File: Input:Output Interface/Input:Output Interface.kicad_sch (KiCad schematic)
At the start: 25 parts, among them J1 Conn_01x03_Male, J2 Conn_01x03_Male, J3 16-way-pcb-edge-Educ-8-connec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, J4 16-way-pcb-edge-Educ-8-connec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, U1 74LS37, U10 74LS01, U11 74LS04, U2 74LS04, U3 7400, U4 74LS04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

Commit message: Schematic update 2024-04-14 plus fixes
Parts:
- C1, C2, C3, C4: value C -> 47nF
- H1, H2: symbol Input:Output-Interface-rescue:Card_handle-EDUC-8 -> EDUC8:Card_handle-EDUC-8
- J3, J4: symbol Input:Output-Interface-rescue:16-way-pcb-edge-Educ-8-connectors-EDUC-8 -> EDUC8:16-way-pcb-edge-Educ-8-connectors-EDUC-8
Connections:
- net I_O_DEVICE_SELECT: now also U3.1, U3.9; no longer U3.12, U3.5
- new net: U2.4, U3.12, U3.5
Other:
- note added: "00"
- note added: "01"
- note added: "10"
- note added: "11"
- note added: "606"
- note added: "616"
- note added: "626"
- note added: "636"
- note added: "C1 47nF C2 47nF C3 47nF C4 47nF H1 Card_handle H2 Card_handle J1 Conn_01x03_Male J2 Conn_01x03_Male J3 16-way-pcb-edge J4 16-way-pcb-edge R1 1K R2 1K R3 1K R4 1K U1 74LS37 U2 74LS04 U3 74LS00 U4 74LS04 U5 74LS00 U6 74LS37 U7 74LS37 U8 74LS01 U9 74LS00 U10 74LS01 U11 74LS04"
- note added: "DATA"
- note added: "c"
- moved on the sheet: C1, C2, C3, C4, H1, H2, J3, J4, U2B, U3D

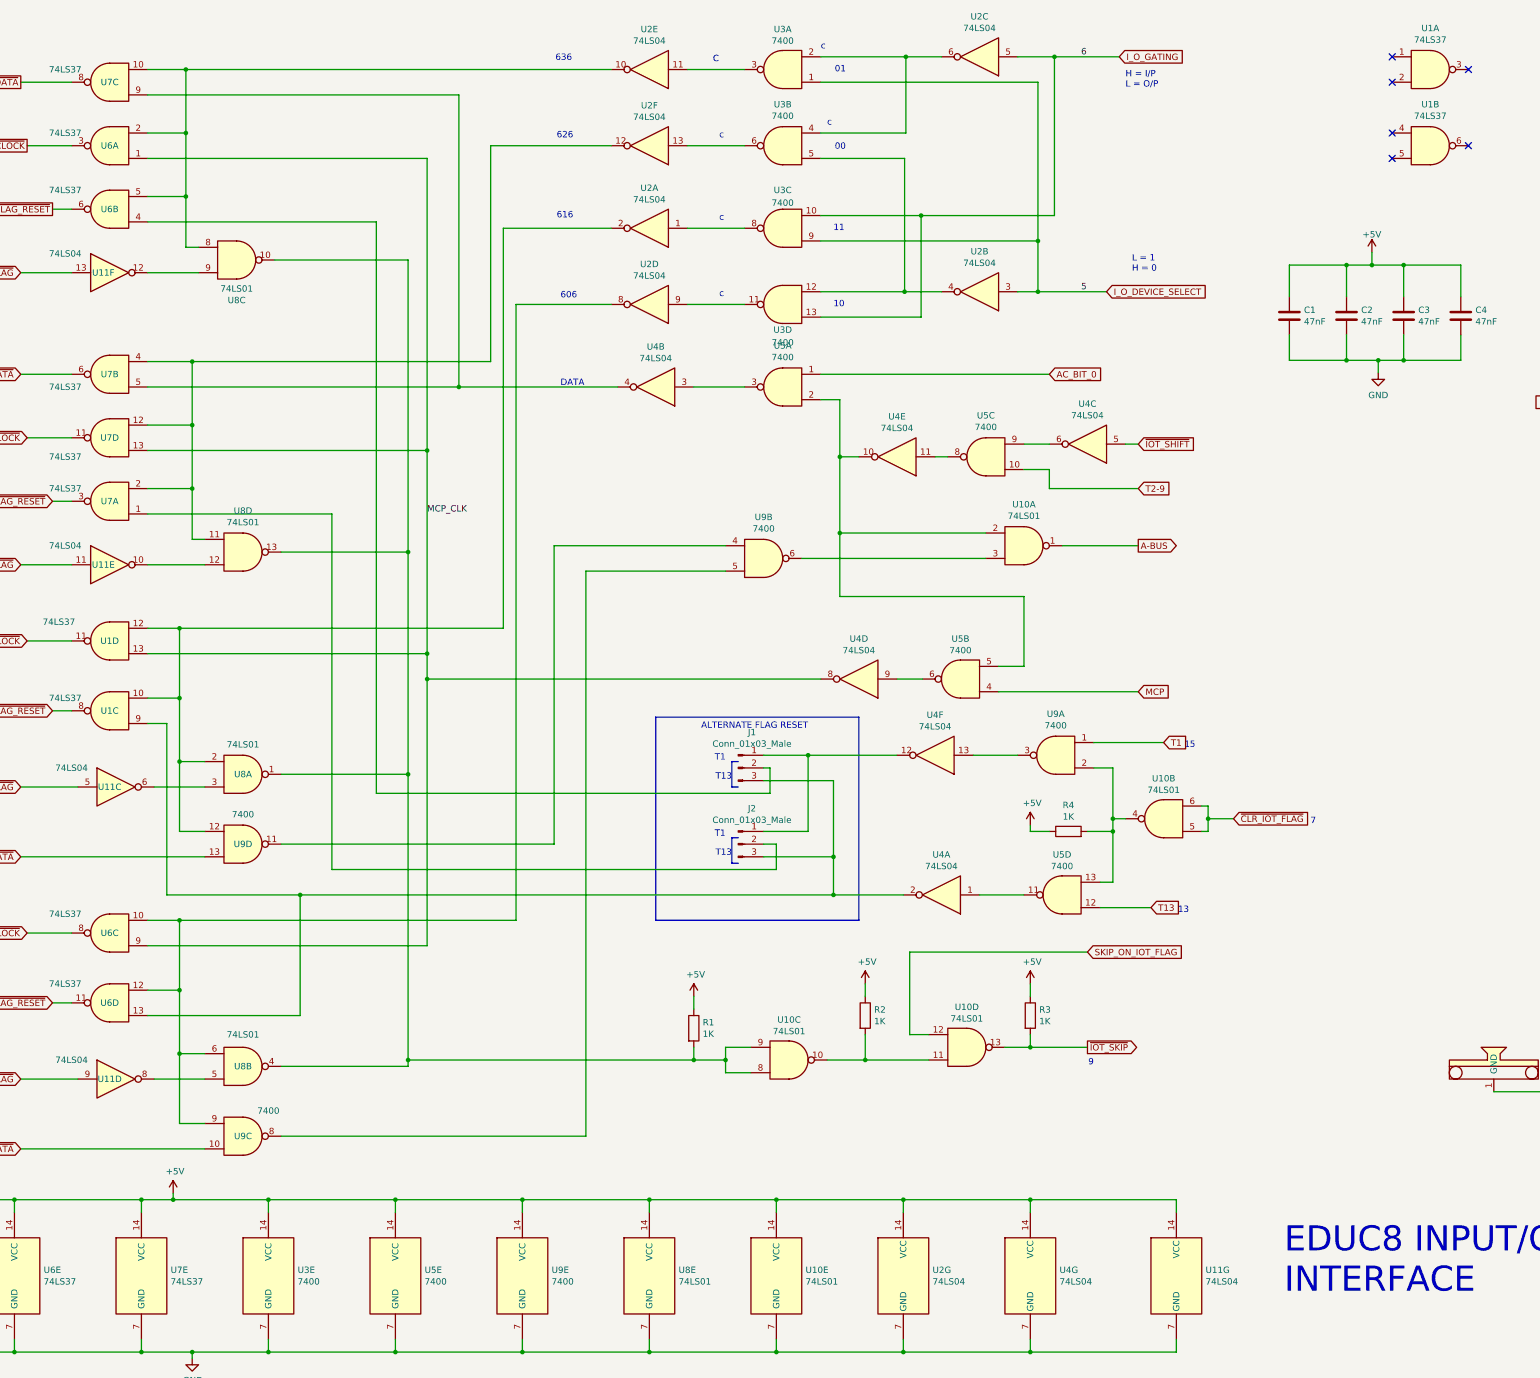
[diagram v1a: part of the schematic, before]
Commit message: Changes 20-7-2025 E8/T. Connected 3 missing supply rail tracks to ICS Added flood fill top and bottom to reduce noise E8/F Corrected labelling on RHS board to reflect EXT_LA not GND Changed fast slow switch operation so fast is in the DOWN position. E8/C. Ran a new track to the 2 pin JST connector from EXT_LA from 10 pin connector on SR input. Added files for E8MX, 2k byte memory expansion board
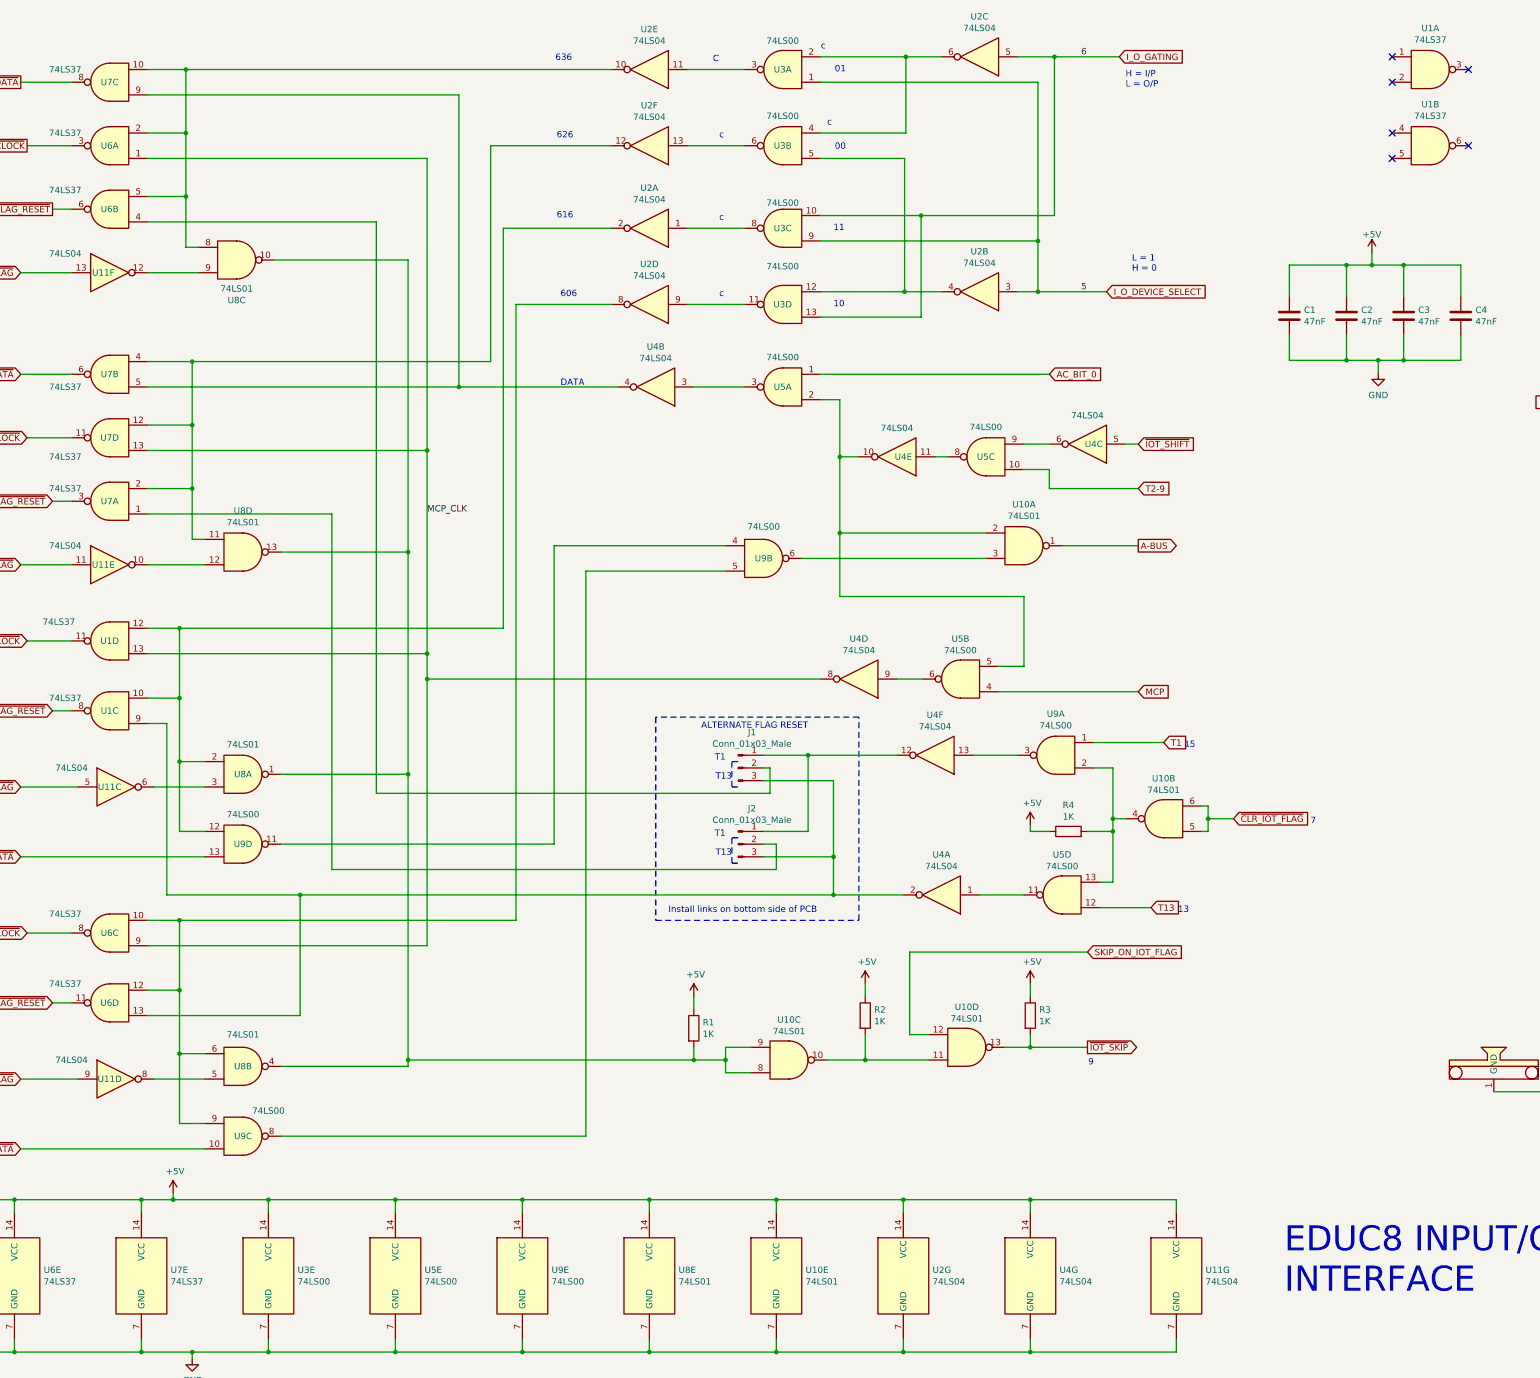
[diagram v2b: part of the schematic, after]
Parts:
- U3, U5, U9: value 7400 -> 74LS00
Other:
- note added: "Install links on bottom side of PCB"
